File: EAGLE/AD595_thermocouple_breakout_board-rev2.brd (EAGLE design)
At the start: 28.6 x 37.3 mm, 5 parts

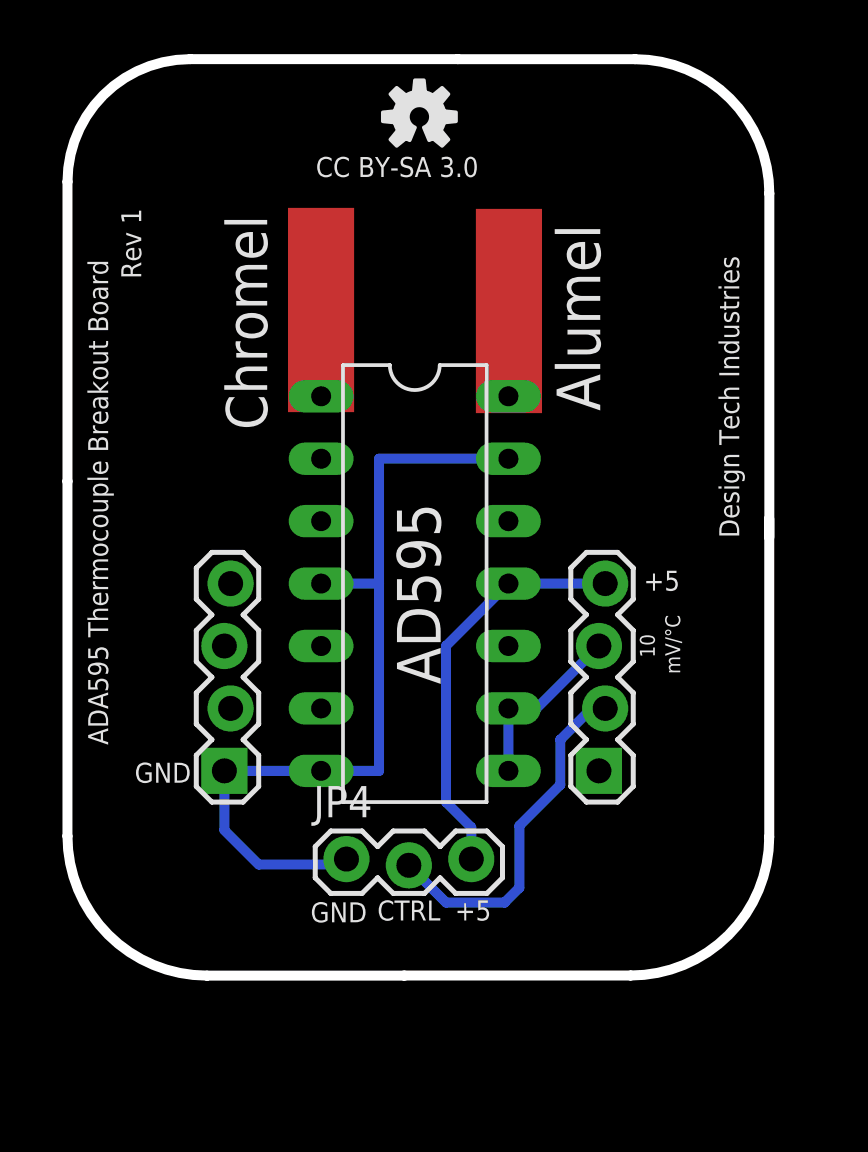
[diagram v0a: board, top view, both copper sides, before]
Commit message: Fix done to board, exposed copper for Thermocouple pads. Added an alarm LED and swapped right-angle headers with 3-pin screw terminal for control signal output.
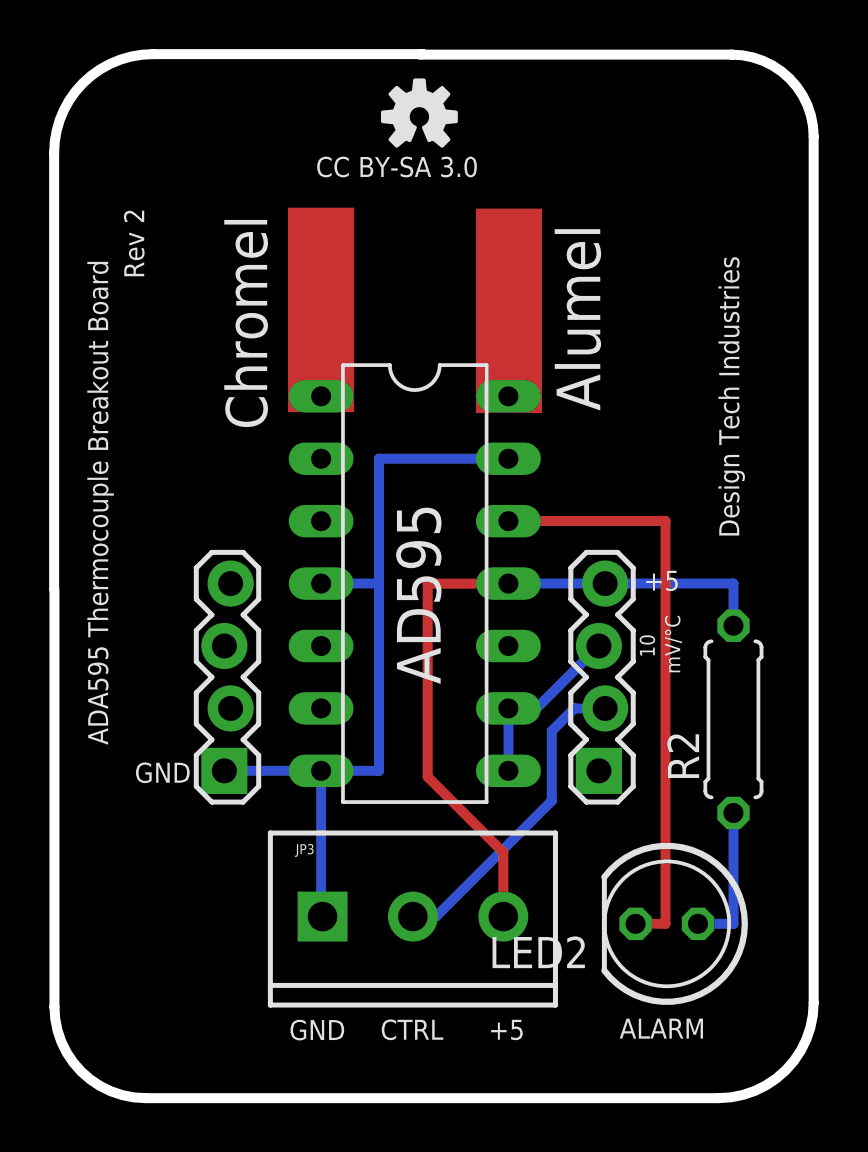
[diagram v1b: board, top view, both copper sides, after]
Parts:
- removed JP4: (no value), SparkFun:1X03_LOCK
- added JP3: (no value), SparkFun-Connectors:SCREWTERMINAL-3.5MM-3_LOCK.007S
- added LED2: (no value), led:LED5MM
- added R2: 330, rcl:0207/7
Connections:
- new net N$7: LED2.A, R2.1
- new net N$8: IC1.12, LED2.K
- net GND: now also JP3.1; no longer JP4.1
- net N$1: now also JP3.2; no longer JP4.2
- net VCC: now also JP3.3, R2.2; no longer JP4.3
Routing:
- net N$8: track 0.00 -> 24.0 mm
- net VCC: track 16.6 -> 29.0 mm
- net N$7: track 0.00 -> 5.95 mm
- net GND: track 34.7 -> 32.6 mm
- net N$1: track 14.4 -> 13.0 mm
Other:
- board size 28.6 x 37.3 mm -> 30.9 x 42.5 mm
- board text added: "ALARM"
- board text added: "Rev 2"
- board text removed: "Rev 1"

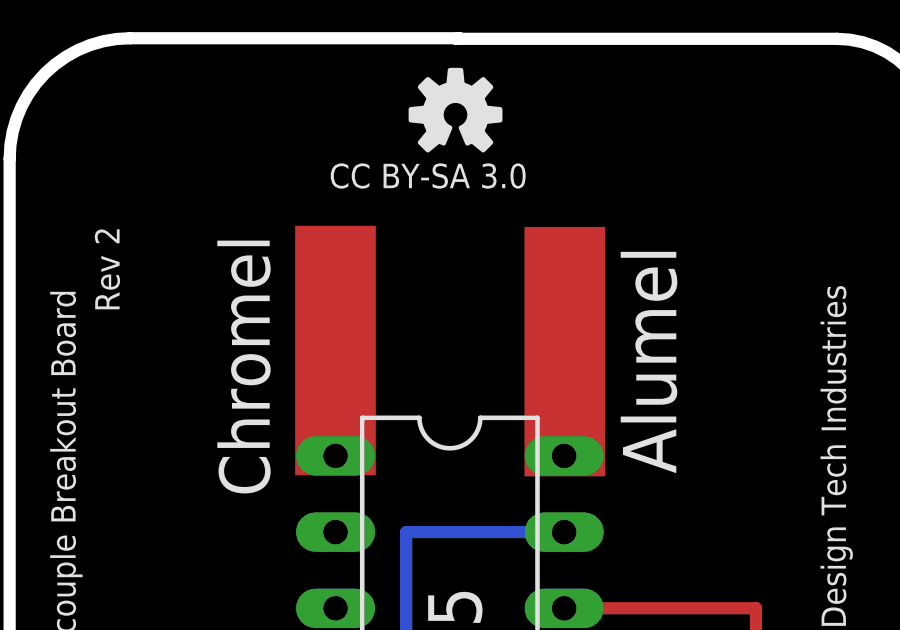
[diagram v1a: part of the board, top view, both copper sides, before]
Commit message: Fix made to Thermocouple solder pads.
I thought I had the problem licked but I didn't. Had to end up throwing
in two large pads per lead to get it to work. I might have to make an
EAGLE library for the 'part' that'll do the job I need.
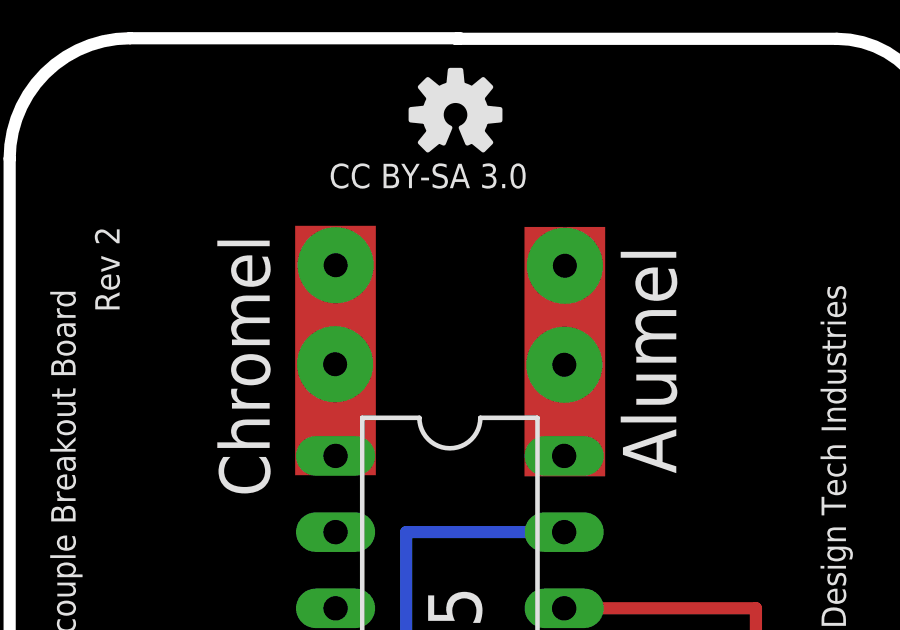
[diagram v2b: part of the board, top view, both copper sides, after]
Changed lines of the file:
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@@
 <wire x1="34.856115625" y1="60.708771875" x2="34.856115625" y2="42.960340625" width="0.4064" layer="20"/>
 <text x="38.521540625" y="55.587390625" size="0.8128" layer="21" rot="R90">Rev 2</text>
-<rectangle x1="44.61865625" y1="51.42545" x2="46.80376875" y2="58.23275" layer="17"/>
-<rectangle x1="52.30185" y1="51.42545" x2="54.45170625" y2="58.197496875" layer="17"/>
-<wire x1="44.8477625" y1="51.6342375" x2="44.8301875" y2="51.6342375" width="0.4064" layer="17"/>
-<wire x1="44.8301875" y1="51.6342375" x2="44.8301875" y2="51.070153125" width="0.4064" layer="17"/>
-<wire x1="46.42693125" y1="51.889559375" x2="46.603209375" y2="51.889559375" width="0.4064" layer="17"/>
-<wire x1="46.603209375" y1="51.889559375" x2="46.603209375" y2="51.25516875" width="0.4064" layer="17"/>
-<wire x1="45.04324375" y1="51.722221875" x2="44.822975" y2="51.722221875" width="0.4064" layer="17"/>
-<wire x1="44.822975" y1="51.722221875" x2="44.822975" y2="50.885140625" width="0.4064" layer="17"/>
-<wire x1="53.821075" y1="52.118665625" x2="54.235196875" y2="52.118665625" width="0.4064" layer="17"/>
-<wire x1="54.235196875" y1="52.118665625" x2="54.235196875" y2="50.7705375" width="0.4064" layer="17"/>
-<wire x1="54.03250625" y1="52.153921875" x2="54.252875" y2="52.153921875" width="0.4064" layer="17"/>
-<wire x1="54.252875" y1="52.153921875" x2="54.252875" y2="50.68245" width="0.4064" layer="17"/>
-<wire x1="52.97495" y1="52.05699375" x2="52.507896875" y2="52.05699375" width="0.4064" layer="17"/>
-<wire x1="52.507896875" y1="52.05699375" x2="52.507896875" y2="51.07899375" width="0.4064" layer="17"/>
 <text x="57.86089375" y="24.665534375" size="0.8128" layer="21">ALARM</text>
 </plain>
@@
 <wire x1="53.34" y1="45.722946875" x2="53.34" y2="45.72" width="0.4064" layer="1"/>
 </signal>
+<signal name="N$9">
+<via x="45.70516875" y="53.85633125" extent="1-16" drill="0.8" diameter="2.54" shape="square"/>
+<via x="45.72274375" y="57.15599375" extent="1-16" drill="0.8" diameter="2.54" shape="square"/>
+<wire x1="45.70516875" y1="53.85633125" x2="45.72274375" y2="57.15599375" width="0" layer="19" extent="1-1"/>
+</signal>
+<signal name="N$3">
+<via x="53.345996875" y="53.838653125" extent="1-16" drill="0.8" diameter="2.54" shape="square"/>
+<via x="53.363571875" y="57.138315625" extent="1-16" drill="0.8" diameter="2.54" shape="square"/>
+<wire x1="53.345996875" y1="53.838653125" x2="53.363571875" y2="57.138315625" width="0" layer="19" extent="1-1"/>
+</signal>
 </signals>
+<errors>
+</errors>
 </board>
 </drawing>
